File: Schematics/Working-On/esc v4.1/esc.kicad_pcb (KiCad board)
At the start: 4 copper layers, 64 x 38 mm, 66 parts, among them IC1 74HCT08BQ,115, IC2 74HCT08BQ,115, J1 AVR-ISP-10, J2 Conn_01x04, J3 74651174R, J4 74651174R, J5 74651174R, J6 74651174R, J7 74651174R, Q1 BSZ0902NS, Q2 BSZ0902NS, Q3 BSZ0902NS, Q4 BSZ0902NS, Q5 BSZ0902NS, Q6 BSZ0902NS, U1 TLV76750DRVx, U2 ATmega328P-M, U3 DRV8300DRGER

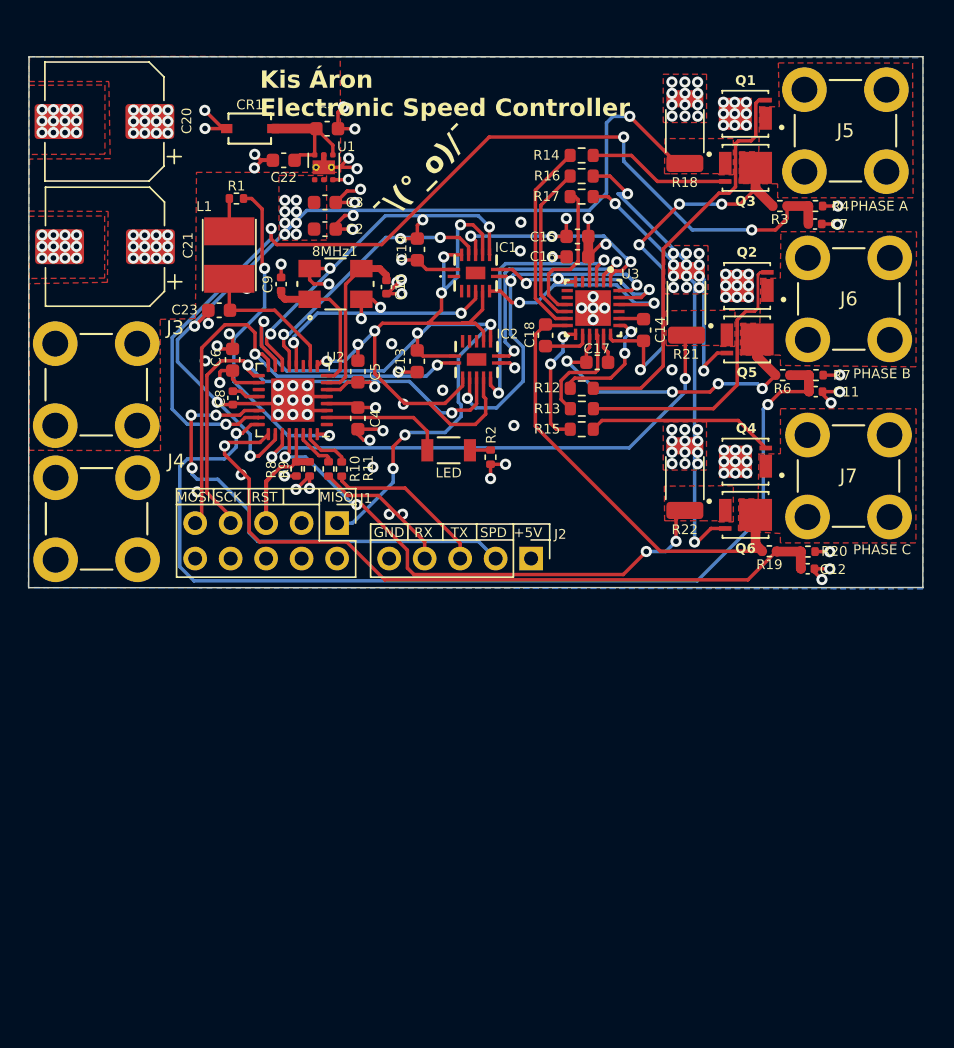
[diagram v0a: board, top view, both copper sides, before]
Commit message: New connectors, and BEMF Filter.
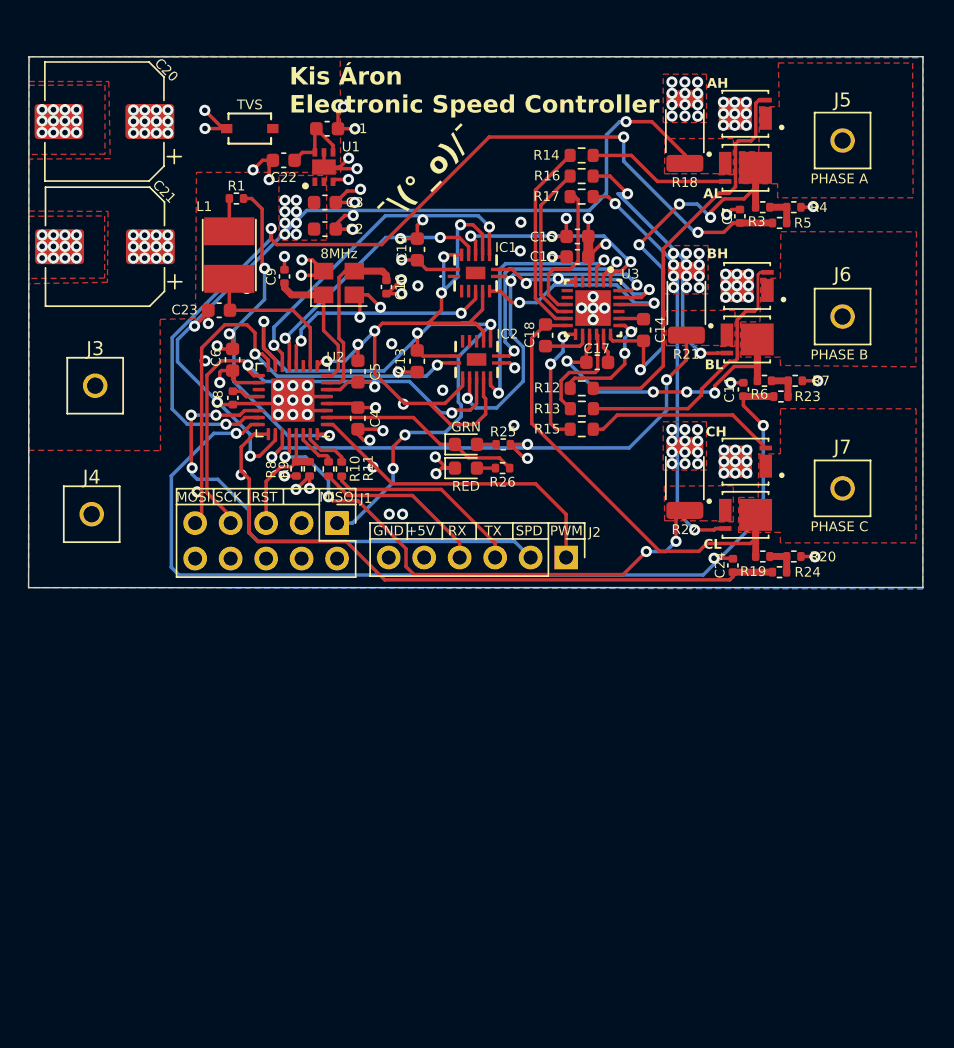
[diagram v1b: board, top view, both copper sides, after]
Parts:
- removed 8MHz1: ECS-80-12-30BQ-JES-TR, ECS-80-12-30BQ-JES-TR:ECS-80-12_ECS
- removed C12: 1n, Capacitor_SMD:C_0402_1005Metric
- removed LED: XZMDKVG55W-4, XZMDKVG55W-4:LED_KVG55W-4_SLD
- removed R2: 300, Resistor_SMD:R_0402_1005Metric
- added 8MHz: ECS-80-12-33-JGN-TR, Crystal:Crystal_SMD_3225-4Pin_3.2x2.5mm, F.Cu at (68.2, 48.2)
- added C24: 2.5n, Capacitor_SMD:C_0402_1005Metric, F.Cu at (96.4, 68.4)
- added GRN: LED, LED_SMD:LED_0603_1608Metric, F.Cu at (77.3, 59.8)
- added R23: 10k, Resistor_SMD:R_0402_1005Metric, F.Cu at (99.8, 56.3)
- added R24: 10k, Resistor_SMD:R_0402_1005Metric, F.Cu at (99.7, 68.9)
- added R25: 300, Resistor_SMD:R_0402_1005Metric, F.Cu at (80.0, 59.8)
- added R26: 300, Resistor_SMD:R_0402_1005Metric, F.Cu at (79.9, 61.5)
- added R5: 10k, Resistor_SMD:R_0402_1005Metric, F.Cu at (99.7, 43.9)
- added RED: LED, LED_SMD:LED_0603_1608Metric, F.Cu at (77.3, 61.5)
- C11: value 1n -> 2.5n
- C7: value 8200pF -> 2.5n
- J2: value Conn_01x04 -> Conn_01x06; footprint Connector_PinHeader_2.54mm:PinHeader_1x05_P2.54mm_Vertical -> Connector_PinHeader_2.54mm:PinHeader_1x06_P2.54mm_Vertical
- J3, J4, J5, J6, J7: value 74651174R -> 8730; footprint 74651174:CONN4_74651174R_WRE -> 8730:8730
- U1: footprint Package_SON:WSON-6-1EP_2x2mm_P0.65mm_EP1x1.6mm_ThermalVias -> TLV76750DRVR:SON65P200X200X80-7N
- moved C7 5.41 mm to (96.9, 43.4), turned to -90 degrees
- moved C11 5.18 mm to (97.2, 55.8), turned to -90 degrees
- moved J6 4.88 mm to (104.2, 50.6)
- moved J7 4.57 mm to (104.2, 62.9)
- moved J5 4.55 mm to (104.2, 38.0)
- moved J3 4.15 mm to (50.8, 55.5)
- moved J4 3.67 mm to (50.5, 64.8)
- moved J2 2.51 mm to (84.5, 67.8)
- moved R4 1.55 mm to (100.8, 42.8)
- moved R7 1.54 mm to (100.9, 55.2)
- moved R6 1.37 mm to (98.7, 55.2)
- moved R3 1.23 mm to (98.5, 42.8)
- moved R20 1.07 mm to (100.8, 67.8)
- moved R19 0.60 mm to (98.5, 67.8)
- moved C9 0.60 mm to (64.3, 47.7)
- renumbered Q1 to AH, Q3 to AL, Q2 to BH, Q5 to BL, Q4 to CH, Q6 to CL, CR1 to TVS
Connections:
- C11 pad 1: COIL_B_BEMF -> GND
- C11 pad 2: GND -> COIL_B_BEMF
- C7 pad 1: COIL_A_BEMF -> GND
- C7 pad 2: GND -> COIL_A_BEMF
- J2 pad 1: +5V -> PWM
- J2 pad 5: GND -> +5V
- R19 pad 1: COIL_C_BEMF -> Net-(R19-Pad1)
- R20 pad 2: COIL_C_BEMF -> Net-(R19-Pad1)
- R3 pad 1: COIL_A_BEMF -> Net-(R3-Pad1)
- R4 pad 2: COIL_A_BEMF -> Net-(R3-Pad1)
- R6 pad 1: COIL_B_BEMF -> Net-(R23-Pad1)
- R7 pad 2: COIL_B_BEMF -> Net-(R23-Pad1)
- U2 pad 1: unconnected-(U2-PD3-Pad1) -> PWM
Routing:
- net PWM: track 0.00 -> 22.9 mm
- net LED: track 8.96 -> 14.6 mm
- net COIL_C_BEMF: track 53.4 -> 48.0 mm, vias 1 -> 0
- net COIL_A_BEMF: track 71.6 -> 66.9 mm
- net GND: track 73.4 -> 77.5 mm, vias 136 -> 135
- net +12V: track 15.2 -> 11.8 mm
- net COIL_B_BEMF: track 72.7 -> 70.0 mm
- net SPEED_REF: track 34.6 -> 37.1 mm
- net TX: track 11.8 -> 14.2 mm
- net RX: track 10.0 -> 12.4 mm
- net Net-(R3-Pad1): track 0.00 -> 2.33 mm
- net Net-(R19-Pad1): track 0.00 -> 2.33 mm
- net Net-(R23-Pad1): track 0.00 -> 2.31 mm
- net COIL_A: track 28.5 -> 30.5 mm
- net Net-(Q5-Pad4): track 21.2 -> 19.4 mm
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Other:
- board text added: "PWM"

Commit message: VIA update
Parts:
- added C12: 47uF, Capacitor_SMD:C_0805_2012Metric, F.Cu at (59.4, 49.1)
- added L2: 100uH, Inductor_SMD:L_0805_2012Metric, F.Cu at (61.3, 49.0)
- C11, C24, C7: value 2.5n -> 2.4n
- C23: value 10uF -> 47uF; footprint Capacitor_SMD:C_0603_1608Metric -> Capacitor_SMD:C_0805_2012Metric
- L1: value 2.2mH -> 100uH; footprint 744045222:WE-LQ_L49 -> Inductor_SMD:L_0805_2012Metric
- R18, R21, R22: value 2m -> 5m
- moved TVS1 18.5 mm to (50.5, 51.8)
- moved C23 4.08 mm to (60.3, 46.1)
- moved L1 3.06 mm to (61.3, 43.3)
- moved J5 2.35 mm to (101.9, 37.9)
- moved J6 2.35 mm to (101.9, 50.5)
- moved J7 2.35 mm to (101.9, 62.8)
- moved C2 1.71 mm to (68.9, 44.2)
- moved C3 1.71 mm to (68.9, 42.3)
- moved C1 1.71 mm to (69.1, 37.0)
- moved U1 1.71 mm to (68.8, 39.8)
- moved C22 1.71 mm to (65.9, 39.3)
- moved R1 1.48 mm to (61.8, 41.0)
- renumbered 8MHz to 8MHz1, GRN to GRN1, AH to Q1, BH to Q2, AL to Q3, CH to Q4, BL to Q5, CL to Q6, RED to RED1, TVS to TVS1
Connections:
- C23 pad 2: COMP_REF_IN -> Net-(C23-Pad2)
- L1 pad 2: COMP_REF_IN -> Net-(C23-Pad2)
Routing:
- net GND: track 77.5 -> 85.5 mm, vias 135 -> 117
- net COIL_B_CURR: track 37.6 -> 41.4 mm
- net Net-(C23-Pad2): track 0.00 -> 3.62 mm
- net Net-(Q1-Pad4): track 29.0 -> 32.4 mm, vias 0 -> 2
- net COIL_A_BEMF: track 66.9 -> 70.2 mm
- net COMP_REF_IN: track 12.9 -> 10.1 mm
- net COIL_C_CURR: track 38.2 -> 40.7 mm
- net COIL_B_BEMF: track 70.0 -> 72.1 mm
- net Net-(Q2-Pad4): track 19.8 -> 21.7 mm, vias 0 -> 2
- net COMP_REF_OUT: track 24.4 -> 26.0 mm
- net +5V: track 23.5 -> 24.9 mm
- net Net-(L1-Pad1): track 2.35 -> 1.22 mm
- net SPEED_REF: track 37.1 -> 38.2 mm
- net AH_PWM: track 15.7 -> 16.7 mm
- net Net-(Q4-Pad4): track 13.7 -> 14.7 mm
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
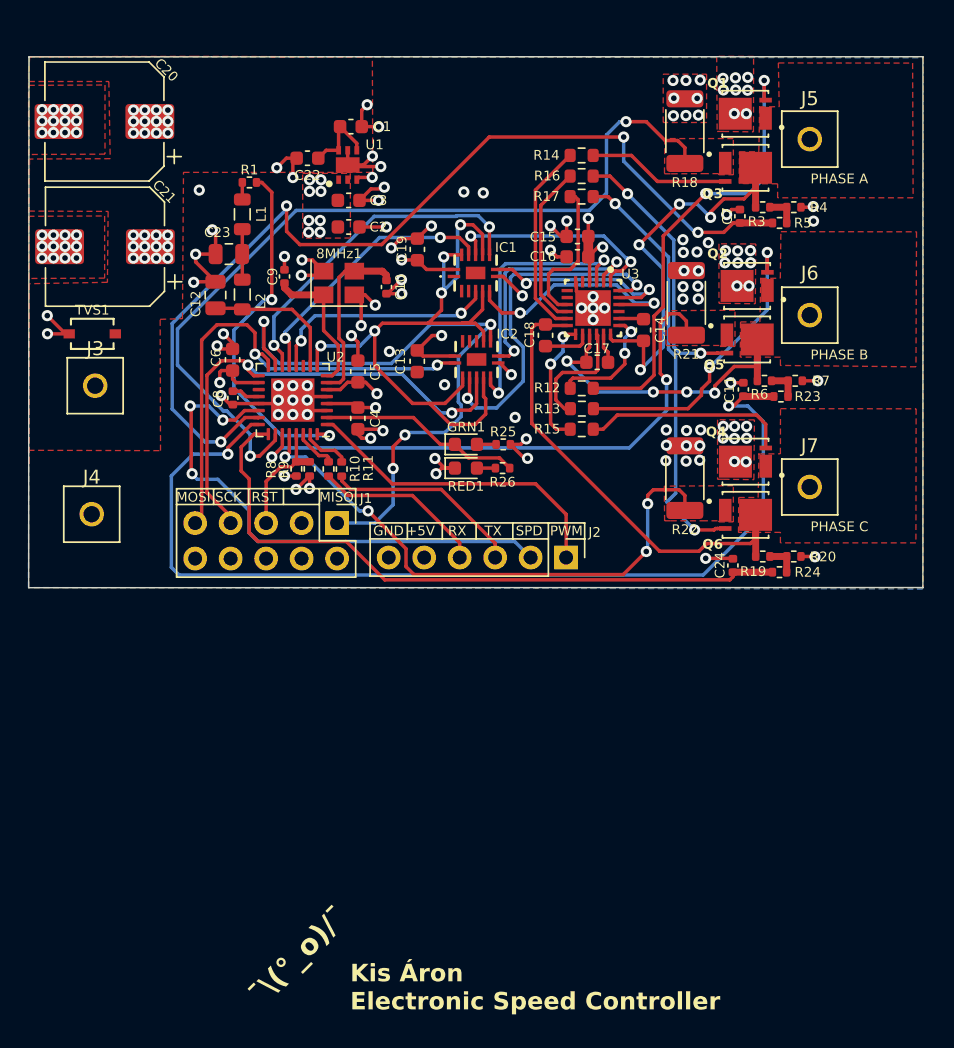
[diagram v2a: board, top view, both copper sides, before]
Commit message: swaped PWM_IN & Comp_Ref_Out, vias finished
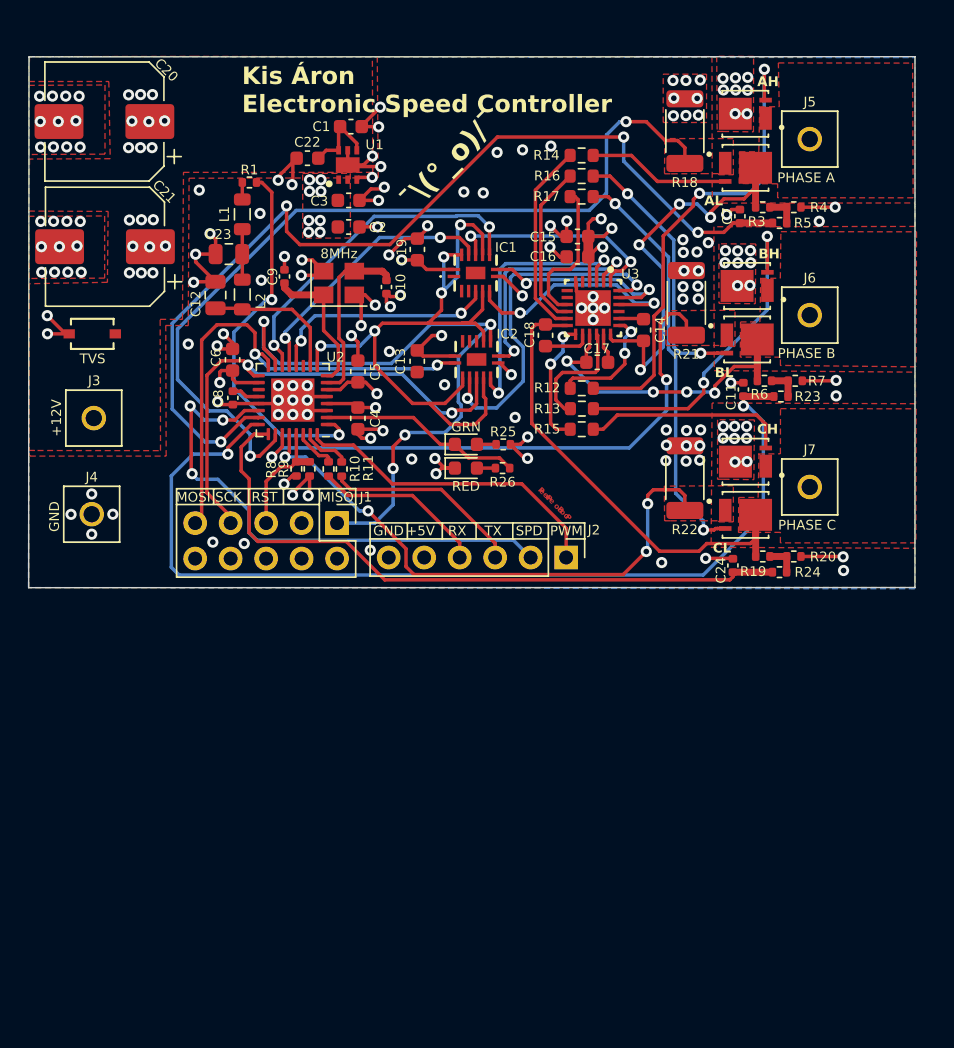
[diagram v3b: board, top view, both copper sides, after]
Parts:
- moved J3 2.32 mm to (50.6, 57.9)
- renumbered 8MHz1 to 8MHz, Q1 to AH, Q3 to AL, Q2 to BH, Q5 to BL, Q4 to CH, Q6 to CL, GRN1 to GRN, RED1 to RED, TVS1 to TVS
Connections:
- J2 pad 1: PWM -> PWM_IN
- U2 pad 1: PWM -> COMP_REF_OUT
- U2 pad 32: COMP_REF_OUT -> PWM_IN
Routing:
- net PWM_IN: track 0.00 -> 22.9 mm
- net PWM: track 22.9 -> 0.00 mm
- net GND: track 85.5 -> 91.7 mm, vias 117 -> 132
- net +12V: track 11.5 -> 14.2 mm, vias 50 -> 45
- net Net-(Q2-Pad4): track 21.7 -> 24.0 mm
- net Net-(Q1-Pad4): track 32.4 -> 34.2 mm
- net COIL_B_BEMF: track 72.1 -> 70.4 mm
- net COMP_REF_OUT: track 26.0 -> 27.1 mm
- net Net-(Q6-Pad4): track 30.3 -> 29.4 mm
- net COIL_A_CURR: track 60.9 -> 61.5 mm
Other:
- board size 64 x 38 mm -> 63.5 x 38 mm
- board text added: "+12V"
- board text added: "P P P P"
- board text added: "ee"
- board text added: "oo"

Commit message: Added pins for the BACK-EMFs and PWM Control signals
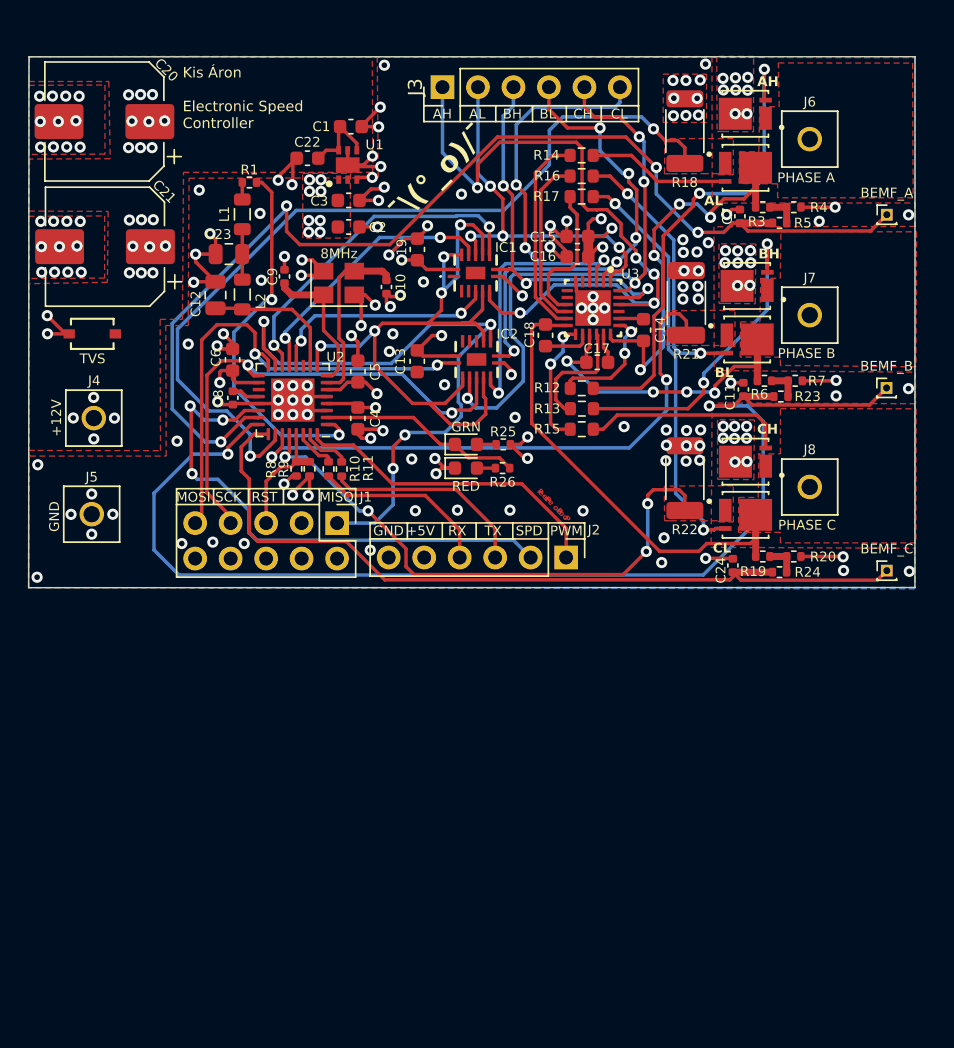
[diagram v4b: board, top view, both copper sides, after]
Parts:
- added BEMF_A: Conn_01x01, Connector_PinHeader_1.00mm:PinHeader_1x01_P1.00mm_Vertical, F.Cu at (107.4, 43.3)
- added BEMF_B: Conn_01x01, Connector_PinHeader_1.00mm:PinHeader_1x01_P1.00mm_Vertical, F.Cu at (107.4, 55.7)
- added BEMF_C: Conn_01x01, Connector_PinHeader_1.00mm:PinHeader_1x01_P1.00mm_Vertical, F.Cu at (107.4, 68.8)
- added J3: Conn_01x06, Connector_PinHeader_2.54mm:PinHeader_1x06_P2.54mm_Vertical, F.Cu at (75.6, 34.2)
- renumbered J3 to J4, J4 to J5, J5 to J6, J6 to J7, J7 to J8
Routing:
- net AH_PWM: track 16.7 -> 49.3 mm, vias 2 -> 5
- net CL_PWM: track 19.8 -> 39.6 mm, vias 2 -> 4
- net BL_PWM: track 17.3 -> 34.6 mm, vias 2 -> 5
- net CH_PWM: track 25.4 -> 42.3 mm, vias 2 -> 4
- net COIL_B_BEMF: track 70.4 -> 86.9 mm
- net BH_PWM: track 14.4 -> 27.9 mm, vias 2 -> 3
- net COIL_C_BEMF: track 48.0 -> 59.5 mm
- net COIL_A_BEMF: track 70.2 -> 81.5 mm
- net AL_PWM: track 16.0 -> 27.2 mm, vias 2 -> 4
- net GND: track 91.7 -> 94.6 mm, vias 132 -> 145
- net Net-(Q2-Pad4): track 24.0 -> 23.0 mm
- net COIL_A: track 30.5 -> 29.6 mm
- net COIL_A_CURR: track 61.5 -> 60.8 mm
- net Net-(U3-GLA): track 14.1 -> 14.8 mm
- net Net-(U3-GLB): track 11.7 -> 12.4 mm
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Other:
- board text added: "AH"
- board text added: "AL"
- board text added: "BH"
- board text added: "BL"
- board text added: "CH"
- board text added: "CL"

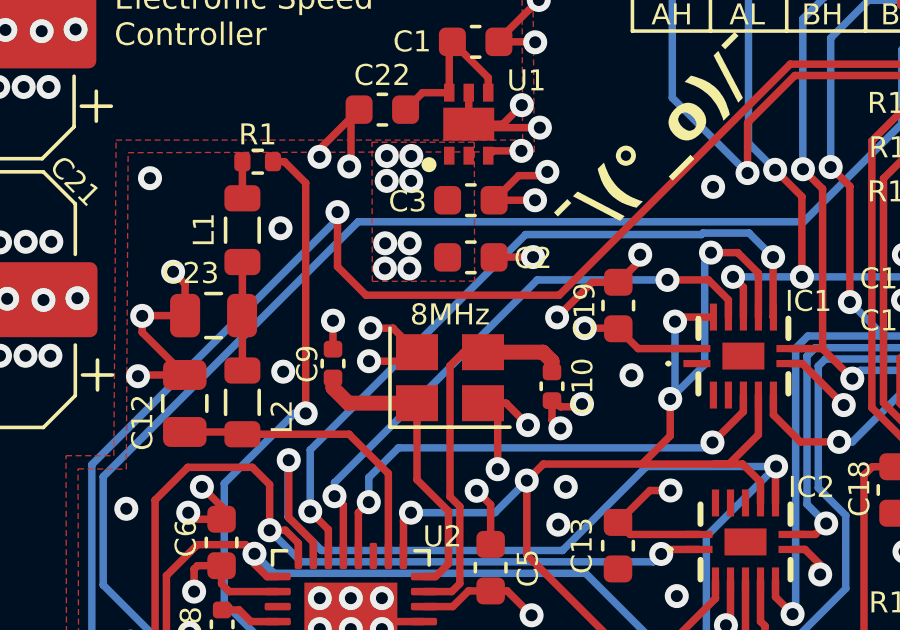
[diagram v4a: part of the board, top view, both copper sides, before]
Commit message: Changed 8MHz to XTAL (might use 16MHz)
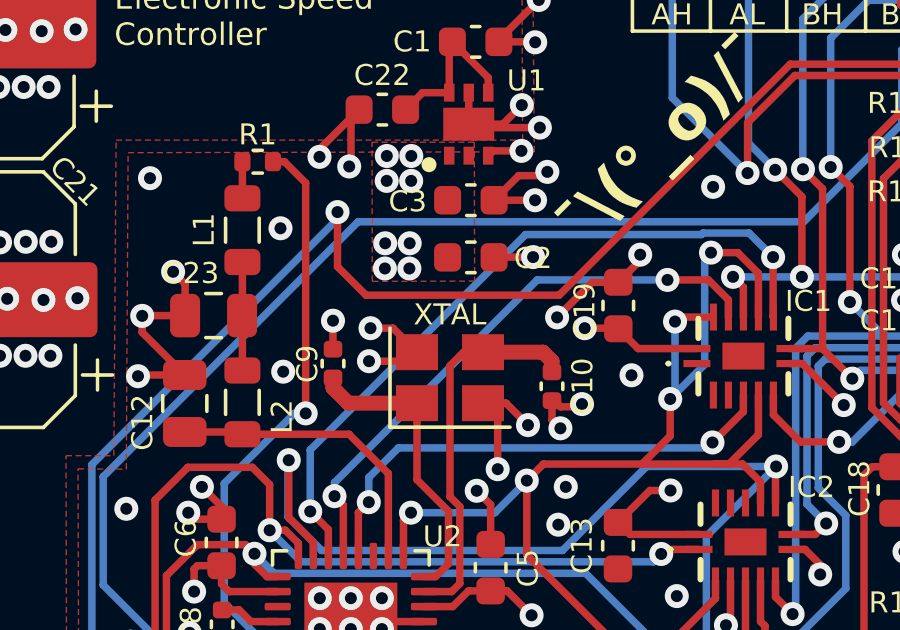
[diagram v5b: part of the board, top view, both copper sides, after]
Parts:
- renumbered 8MHz to XTAL
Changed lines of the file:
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@@
 		(descr "SMD Crystal SERIES SMD3225/4 http://www.txccrystal.com/images/pdf/7m-accuracy.pdf, 3.2x2.5mm^2 package")
 		(tags "SMD SMT crystal")
-		(property "Reference" "8MHz"
+		(property "Reference" "XTAL"
 			(at 0 -2.1 0)
 			(layer "F.SilkS")
